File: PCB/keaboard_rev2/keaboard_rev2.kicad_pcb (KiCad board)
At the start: 2 copper layers, 141.9 x 93.7 mm, 78 parts, among them J1 AudioJack4, SW1 SW_Push, SW10 SW_Push, SW11 SW_Push, SW12 SW_Push, SW13 SW_Push, SW14 SW_Push, SW15 SW_Push, SW16 SW_Push, SW17 SW_Push, SW18 SW_Push, SW19 SW_Push, SW2 SW_Push, SW20 SW_Push, SW21 SW_Push, SW22 SW_Push, SW23 SW_Push, SW24 SW_Push, SW25 SW_Push, SW3 SW_Push, SW4 SW_Push, SW5 SW_Push, SW6 SW_Push, SW7 SW_Push, SW8 SW_Push, SW9 SW_Push, U1 ProMicro

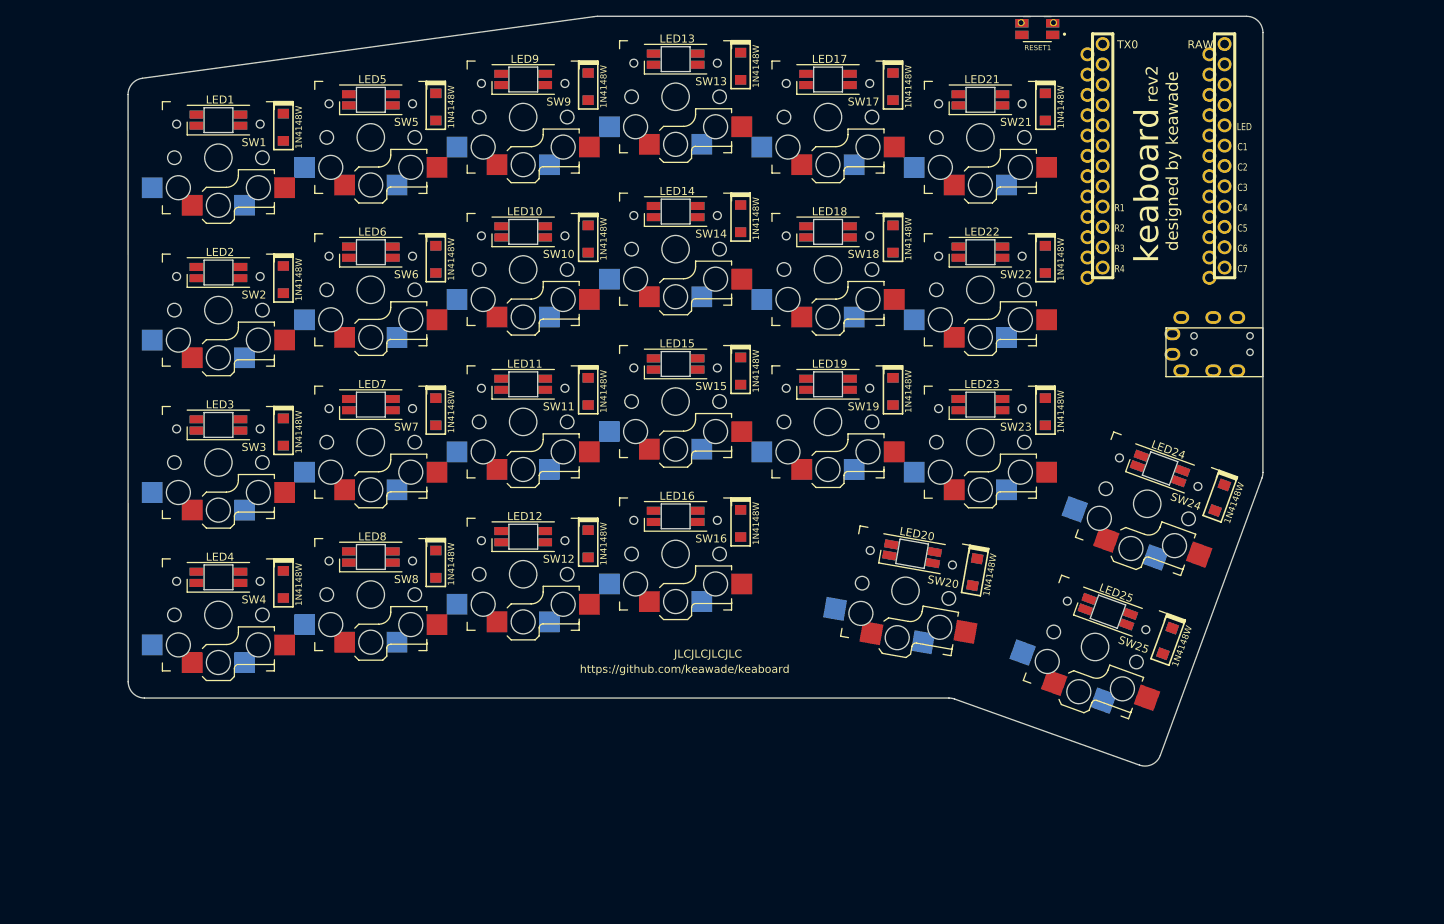
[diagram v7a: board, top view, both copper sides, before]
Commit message: Better footprints, OLED, misc
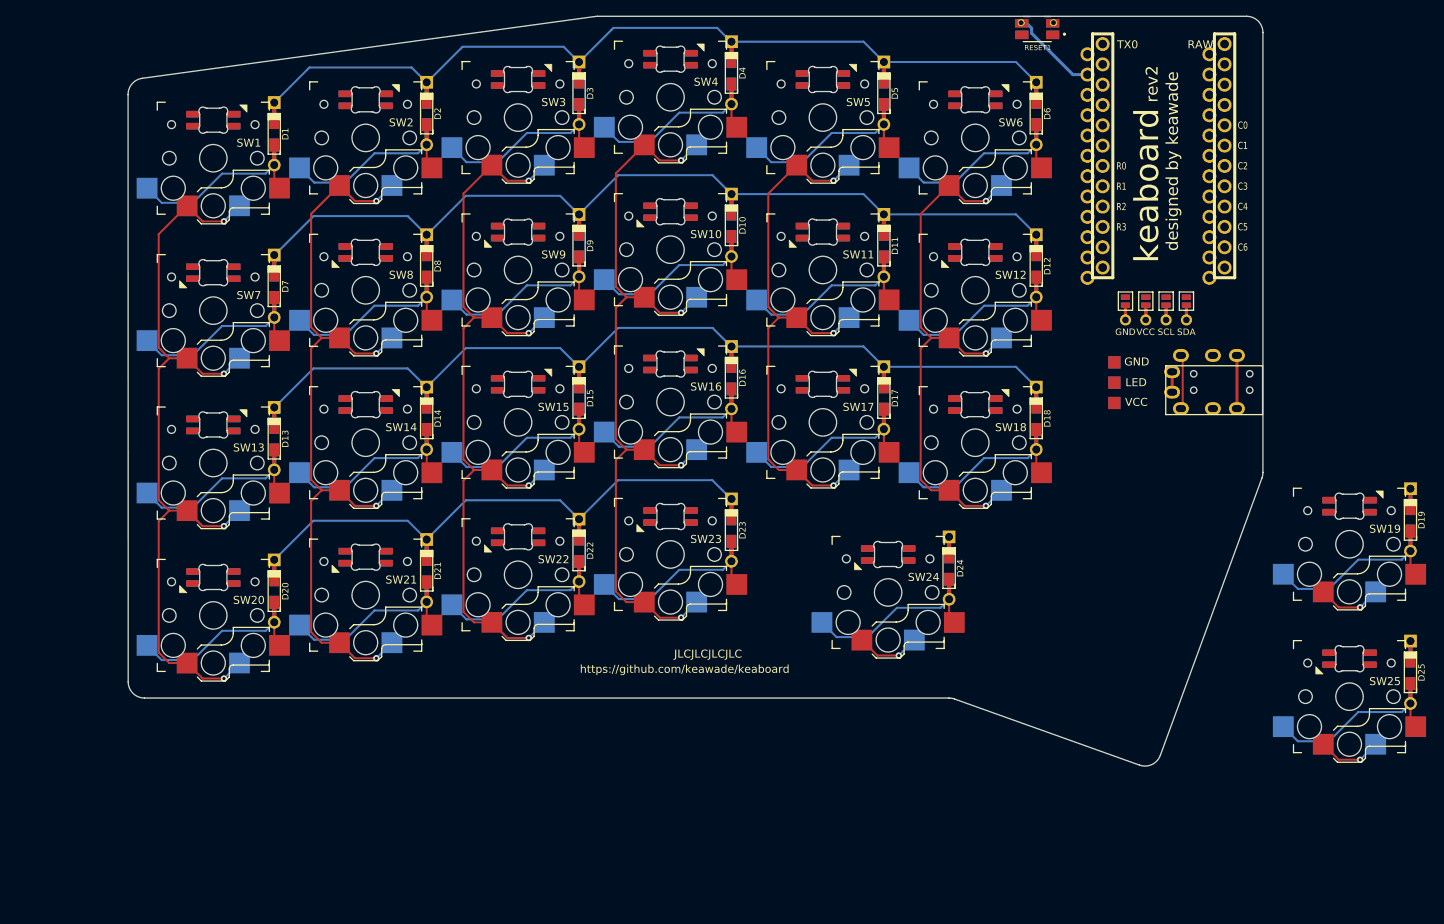
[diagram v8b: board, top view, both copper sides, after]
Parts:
- added JP1: GND, kbd:Jumper, F.Cu at (168.5, 75.0)
- added JP2: VCC, kbd:Jumper, F.Cu at (171.0, 75.0)
- added JP3: SCL, kbd:Jumper, F.Cu at (173.6, 75.0)
- added JP4: SDA, kbd:Jumper, F.Cu at (176.1, 75.0)
- added JP5: SDA, kbd:Jumper, B.Cu at (168.5, 75.0)
- added JP6: SCL, kbd:Jumper, B.Cu at (171.0, 75.0)
- added JP7: VCC, kbd:Jumper, B.Cu at (173.6, 75.0)
- added JP8: GND, kbd:Jumper, B.Cu at (176.1, 75.0)
- added P1: OLED, kbd:OLED_v2, F.Cu at (172.3, 77.4)
- added P2: LED, parts:StripLED_reversible, F.Cu at (167.1, 87.8)
- D1, D10, D11, D12, D13, D14, D15, D16, D17, D18, D19, D2, D20, D21, D22, D23, D24, D25, D3, D4, D5, D6, D7, D8, D9: value 1N4148W -> D; footprint parts:D_SOD123_reversible -> Keebio-Parts:Diode-dual
- LED1, LED10, LED11, LED12, LED13, LED14, LED15, LED16, LED17, LED18, LED19, LED2, LED20, LED21, LED22, LED23, LED24, LED25, LED3, LED4, LED5, LED6, LED7, LED8, LED9: value SK6812MINI -> SK6812MINI-E; footprint parts:YS-SK6812MINI-E_reversible -> parts:SK6812MINI-E_reversible
- moved D21 96.7 mm to (81.2, 108.7)
- moved SW21 95.8 mm to (73.5, 111.8)
- moved LED21 95.8 mm to (73.5, 107.0), turned to 180 degrees
- moved D20 87.6 mm to (62.1, 111.3), turned to 90 degrees
- moved LED20 87.4 mm to (54.5, 109.6), turned to 180 degrees
- moved SW20 86.6 mm to (54.5, 114.3), turned to 0 degrees
- moved LED4 86.0 mm to (111.6, 44.8)
- moved SW4 85.9 mm to (111.6, 49.5)
- moved D4 85.0 mm to (119.3, 46.5)
- moved LED6 77.9 mm to (149.7, 49.9)
- moved SW6 77.9 mm to (149.7, 54.6)
- moved D6 77.2 mm to (157.4, 51.6)
- moved D13 74.6 mm to (62.1, 92.2)
- moved SW13 73.7 mm to (54.5, 95.3)
- moved LED13 73.7 mm to (54.5, 90.5)
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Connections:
- D1 pad 1: Row1 -> Row0
- D10 pad 1: Row2 -> Row1
- D11 pad 1: Row3 -> Row1
- D12 pad 1: Row4 -> Row1
- D13 pad 1: Row1 -> Row2
- D15 pad 1: Row3 -> Row2
- D16 pad 1: Row4 -> Row2
- D17 pad 1: Row1 -> Row2
- D19 pad 1: Row3 -> Row2
- D2 pad 1: Row2 -> Row0
- D20 pad 1: Row4 -> Row3
- D21 pad 1: Row1 -> Row3
- D22 pad 1: Row2 -> Row3
- D25 pad 1: Row4 -> Row3
- D3 pad 1: Row3 -> Row0
- D4 pad 1: Row4 -> Row0
- D5 pad 1: Row1 -> Row0
- D6 pad 1: Row2 -> Row0
- D7 pad 1: Row3 -> Row1
- D8 pad 1: Row4 -> Row1
- J1 pad R2: TRRS_R2 -> GND
- J1 pad S: GND -> VCC
- J1 pad T: TRRS_T -> DATA
- LED1 pad 1: Net-(LED1-Pad1) -> VCC
- LED1 pad 2: RAW -> Net-(LED1-Pad2)
- LED1 pad 3: Net-(LED1-Pad3) -> GND
- LED1 pad 4: GND -> Net-(LED1-Pad4)
- LED10 pad 1: Net-(LED10-Pad1) -> VCC
- LED10 pad 2: RAW -> Net-(LED10-Pad2)
- LED10 pad 3: Net-(LED10-Pad3) -> GND
- LED10 pad 4: GND -> Net-(LED10-Pad4)
- LED11 pad 1: Net-(LED11-Pad1) -> VCC
- LED11 pad 2: RAW -> Net-(LED11-Pad2)
- LED11 pad 3: Net-(LED11-Pad3) -> GND
- LED11 pad 4: GND -> Net-(LED10-Pad2)
- LED12 pad 1: Net-(LED12-Pad1) -> VCC
- LED12 pad 2: RAW -> Net-(LED12-Pad2)
- LED12 pad 3: Net-(LED12-Pad3) -> GND
- LED12 pad 4: GND -> Net-(LED11-Pad2)
- LED13 pad 1: Net-(LED13-Pad1) -> VCC
- LED13 pad 2: RAW -> Net-(LED13-Pad2)
- LED13 pad 3: Net-(LED13-Pad3) -> GND
- LED13 pad 4: GND -> Net-(LED13-Pad4)
- LED14 pad 1: Net-(LED14-Pad1) -> VCC
- LED14 pad 2: RAW -> Net-(LED13-Pad4)
- LED14 pad 3: Net-(LED10-Pad1) -> GND
- LED14 pad 4: GND -> Net-(LED14-Pad4)
- LED15 pad 1: Net-(LED11-Pad3) -> VCC
- LED15 pad 2: RAW -> Net-(LED14-Pad4)
- LED15 pad 3: Net-(LED15-Pad3) -> GND
- LED15 pad 4: GND -> Net-(LED15-Pad4)
- LED16 pad 1: Net-(LED16-Pad1) -> VCC
- LED16 pad 2: RAW -> Net-(LED15-Pad4)
- LED16 pad 3: Net-(LED12-Pad1) -> GND
- LED16 pad 4: GND -> Net-(LED16-Pad4)
- LED17 pad 1: Net-(LED13-Pad3) -> VCC
- LED17 pad 2: RAW -> Net-(LED16-Pad4)
- LED17 pad 3: Net-(LED17-Pad3) -> GND
- LED17 pad 4: GND -> Net-(LED17-Pad4)
- LED18 pad 1: Net-(LED18-Pad1) -> VCC
- LED18 pad 2: RAW -> Net-(LED17-Pad4)
- LED18 pad 3: Net-(LED14-Pad1) -> GND
- LED18 pad 4: GND -> Net-(LED18-Pad4)
- LED19 pad 1: Net-(LED15-Pad3) -> VCC
- LED19 pad 2: RAW -> Net-(LED18-Pad4)
- LED19 pad 3: Net-(LED19-Pad3) -> GND
- LED19 pad 4: GND -> Net-(LED12-Pad2)
- LED2 pad 1: Net-(LED2-Pad1) -> VCC
- LED2 pad 2: RAW -> Net-(LED1-Pad4)
- LED2 pad 3: Net-(LED1-Pad1) -> GND
- LED2 pad 4: GND -> Net-(LED2-Pad4)
- LED20 pad 1: Net-(LED20-Pad1) -> VCC
- LED20 pad 2: RAW -> Net-(LED20-Pad2)
- LED20 pad 3: Net-(LED16-Pad1) -> GND
- LED20 pad 4: GND -> Net-(LED13-Pad2)
- LED21 pad 1: Net-(LED17-Pad3) -> VCC
- LED21 pad 2: RAW -> Net-(LED21-Pad2)
- LED21 pad 3: LED -> GND
- LED21 pad 4: GND -> Net-(LED20-Pad2)
- LED22 pad 1: Net-(LED22-Pad1) -> VCC
- LED22 pad 2: RAW -> Net-(LED22-Pad2)
- LED22 pad 3: Net-(LED18-Pad1) -> GND
- LED22 pad 4: GND -> Net-(LED21-Pad2)
- LED23 pad 1: Net-(LED19-Pad3) -> VCC
- LED23 pad 2: RAW -> Net-(LED23-Pad2)
- LED23 pad 3: Net-(LED22-Pad1) -> GND
- LED23 pad 4: GND -> Net-(LED22-Pad2)
- LED24 pad 1: Net-(LED24-Pad1) -> VCC
- LED24 pad 2: RAW -> Net-(LED24-Pad2)
- LED24 pad 3: Net-(LED24-Pad3) -> GND
- LED24 pad 4: GND -> Net-(LED23-Pad2)
- LED25 pad 1: Net-(LED24-Pad3) -> VCC
- LED25 pad 2: RAW -> Net-(LED25-Pad2)
- LED25 pad 3: Net-(LED20-Pad1) -> GND
- LED25 pad 4: GND -> Net-(LED24-Pad2)
- LED3 pad 1: Net-(LED3-Pad1) -> VCC
- LED3 pad 2: RAW -> Net-(LED2-Pad4)
- LED3 pad 3: Net-(LED3-Pad3) -> GND
- LED3 pad 4: GND -> Net-(LED3-Pad4)
- LED4 pad 1: Net-(LED4-Pad1) -> VCC
- LED4 pad 2: RAW -> Net-(LED3-Pad4)
- LED4 pad 3: Net-(LED3-Pad1) -> GND
- LED4 pad 4: GND -> Net-(LED4-Pad4)
- LED5 pad 1: Net-(LED1-Pad3) -> VCC
- LED5 pad 2: RAW -> Net-(LED4-Pad4)
- LED5 pad 3: Net-(LED5-Pad3) -> GND
- LED5 pad 4: GND -> Net-(LED5-Pad4)
- LED6 pad 1: Net-(LED10-Pad3) -> VCC
- LED6 pad 2: RAW -> Net-(LED5-Pad4)
- LED6 pad 3: Net-(LED6-Pad3) -> GND
- LED6 pad 4: GND -> LED
- LED7 pad 1: Net-(LED3-Pad3) -> VCC
- LED7 pad 2: RAW -> Net-(LED7-Pad2)
- LED7 pad 3: Net-(LED11-Pad1) -> GND
- LED7 pad 4: GND -> Net-(LED1-Pad2)
- LED8 pad 1: Net-(LED12-Pad3) -> VCC
- LED8 pad 2: RAW -> Net-(LED8-Pad2)
- LED8 pad 3: Net-(LED4-Pad1) -> GND
- LED8 pad 4: GND -> Net-(LED7-Pad2)
- LED9 pad 1: Net-(LED5-Pad3) -> VCC
- LED9 pad 2: RAW -> Net-(LED10-Pad4)
- LED9 pad 3: Net-(LED13-Pad1) -> GND
- LED9 pad 4: GND -> Net-(LED8-Pad2)
- SW1 pad 1: Net-(D1-Pad2) -> Col0
- SW1 pad 2: Col1 -> Net-(D1-Pad2)
- SW10 pad 1: Net-(D10-Pad2) -> Col3
- SW10 pad 2: Col3 -> Net-(D10-Pad2)
- SW11 pad 1: Net-(D11-Pad2) -> Col4
- SW11 pad 2: Col3 -> Net-(D11-Pad2)
- SW12 pad 1: Net-(D12-Pad2) -> Col5
- SW12 pad 2: Col3 -> Net-(D12-Pad2)
- SW13 pad 1: Net-(D13-Pad2) -> Col0
- SW13 pad 2: Col4 -> Net-(D13-Pad2)
- SW14 pad 1: Net-(D14-Pad2) -> Col1
- SW14 pad 2: Col4 -> Net-(D14-Pad2)
- SW15 pad 1: Net-(D15-Pad2) -> Col2
- SW15 pad 2: Col4 -> Net-(D15-Pad2)
- SW16 pad 1: Net-(D16-Pad2) -> Col3
- SW16 pad 2: Col4 -> Net-(D16-Pad2)
- SW17 pad 1: Net-(D17-Pad2) -> Col4
- SW17 pad 2: Col5 -> Net-(D17-Pad2)
- SW18 pad 1: Net-(D18-Pad2) -> Col5
- SW18 pad 2: Col5 -> Net-(D18-Pad2)
- SW19 pad 1: Net-(D19-Pad2) -> Col6
- SW19 pad 2: Col5 -> Net-(D19-Pad2)
- SW2 pad 1: Net-(D2-Pad2) -> Col1
- SW2 pad 2: Col1 -> Net-(D2-Pad2)
- SW20 pad 1: Net-(D20-Pad2) -> Col0
- SW20 pad 2: Col5 -> Net-(D20-Pad2)
- SW21 pad 1: Net-(D21-Pad2) -> Col1
- SW21 pad 2: Col6 -> Net-(D21-Pad2)
- SW22 pad 1: Net-(D22-Pad2) -> Col2
- SW22 pad 2: Col6 -> Net-(D22-Pad2)
- SW23 pad 1: Net-(D23-Pad2) -> Col3
- SW23 pad 2: Col6 -> Net-(D23-Pad2)
- SW24 pad 1: Net-(D24-Pad2) -> Col4
- SW24 pad 2: Col7 -> Net-(D24-Pad2)
- SW25 pad 1: Net-(D25-Pad2) -> Col6
- SW25 pad 2: Col7 -> Net-(D25-Pad2)
- SW3 pad 1: Net-(D3-Pad2) -> Col2
- SW3 pad 2: Col1 -> Net-(D3-Pad2)
- SW4 pad 1: Net-(D4-Pad2) -> Col3
- SW4 pad 2: Col1 -> Net-(D4-Pad2)
- SW5 pad 1: Net-(D5-Pad2) -> Col4
- SW5 pad 2: Col2 -> Net-(D5-Pad2)
- SW6 pad 1: Net-(D6-Pad2) -> Col5
- SW6 pad 2: Col2 -> Net-(D6-Pad2)
- SW7 pad 1: Net-(D7-Pad2) -> Col0
- SW7 pad 2: Col2 -> Net-(D7-Pad2)
- SW8 pad 1: Net-(D8-Pad2) -> Col1
- SW8 pad 2: Col2 -> Net-(D8-Pad2)
- SW9 pad 1: Net-(D9-Pad2) -> Col2
- SW9 pad 2: Col3 -> Net-(D9-Pad2)
- U1 pad 1: Net-(U1-Pad1) -> LED
- U1 pad 10: Row2 -> Row3
- U1 pad 11: Row3 -> Net-(U1-Pad11)
- U1 pad 12: Row4 -> Net-(U1-Pad12)
- U1 pad 13: Col7 -> Net-(U1-Pad13)
- U1 pad 2: Net-(U1-Pad2) -> DATA
- U1 pad 20: Net-(U1-Pad20) -> Col0
- U1 pad 21: TRRS_R2 -> VCC
- U1 pad 24: RAW -> VCC
- U1 pad 5: Net-(U1-Pad5) -> SCL
- U1 pad 6: TRRS_T -> SDA
- U1 pad 7: Net-(U1-Pad7) -> Row0
- U1 pad 8: LED -> Row1
- U1 pad 9: Row1 -> Row2
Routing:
- net Row2: track 0.00 -> 106.3 mm
- net Row1: track 0.00 -> 106.3 mm
- net Row0: track 0.00 -> 105.1 mm
- net Col0: track 0.00 -> 100.7 mm, vias 0 -> 4
- net Col3: track 0.00 -> 100.7 mm, vias 0 -> 4
- net Col2: track 0.00 -> 100.7 mm, vias 0 -> 4
- net Col1: track 0.00 -> 100.7 mm, vias 0 -> 4
- net Col4: track 0.00 -> 78.3 mm, vias 0 -> 4
- net Col5: track 0.00 -> 70.2 mm, vias 0 -> 3
- net Row3: track 0.00 -> 66.1 mm
- net Net-(D19-Pad2): track 0.00 -> 21.8 mm
- net Net-(D12-Pad2): track 0.00 -> 21.8 mm
- net Net-(D8-Pad2): track 0.00 -> 21.8 mm
- net Net-(D20-Pad2): track 0.00 -> 21.8 mm
- net Net-(D6-Pad2): track 0.00 -> 21.8 mm
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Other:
- board text added: "C0"
- board text added: "R0"
- board text removed: "C7"
- board text removed: "LED"
- board text removed: "R4"
